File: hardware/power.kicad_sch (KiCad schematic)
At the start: 0 parts

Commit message: schematic: power and imu sheets drawn (ERC 0 on each sheet; P4-1/2/3/7/9/12/17/19 closed in block notes)
Co-Authored-By: Claude Opus 5.5 <noreply@anthropic.com>
Claude-Session: https://claude.ai/code/session_01RFaS5jnC9tnPam9GBgmGnG
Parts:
- added C1, C10, C11, C2, C7, C8, C9: 22uF, lib:C_0603_1608Metric_W, symbol Device:C
- added C12, C128, C13, C15, C30: 10uF, lib:C_0402_1005Metric_W, symbol Device:C
- added C129, C131, C6: 100nF, lib:C_0201_0603Metric_W, symbol Device:C
- added C14, C17, C5: 1uF, lib:C_0201_0603Metric_W, symbol Device:C
- added C16: 10nF, lib:C_0201_0603Metric_W, symbol Device:C
- added D1: SMF5.0A, lib:SOD-123FL_L2.7-W1.8-LS3.7-RD_Dense, symbol Device:D_Zener
- added D2: BAS16LD, lib:Nexperia_SOD882D, symbol Device:D
- added FB1: 120R@100MHz 0.9A, lib:L_0201_0603Metric_W, symbol Device:FerriteBead
- added L1: 0.68uH 6.5A, lib:IND-SMD_L2.5-W2.0_FTC252012, symbol Device:L
- added R1: 0.5mR 2W, lib:R_1206_Kelvin_4Pad_NetTie_HCS1206_Dense, symbol Device:R_Shunt
- added R10: 18k, lib:R_0201_0603Metric_W, symbol Device:R
- added R11: 2.4k, lib:R_0201_0603Metric_W, symbol Device:R
- added R2, R3: 1k, lib:R_0201_0603Metric_W, symbol Device:R
- added R4: 47k, lib:R_0201_0603Metric_W, symbol Device:R
- added R5: 6.2k, lib:R_0201_0603Metric_W, symbol Device:R
- added R7: 27.4k, lib:R_0201_0603Metric_W, symbol Device:R
- added R8: 10k, lib:R_0201_0603Metric_W, symbol Device:R
- added R87: 510k, lib:R_0201_0603Metric_W, symbol Device:R
- added R9: 33k, lib:R_0201_0603Metric_W, symbol Device:R
- added U1: INA186A3, lib:SOT-363_SC-70-6_Dense, symbol OpenDrone:INA186A3IDCKR
- added U2: TPS61022, lib:TI_VQFN-HR-7_2x2mm_RWU, symbol lib:TPS61022RWUR
- added U24: SGM40661, lib:WLCSP-6_L1.30-W0.94-P0.40_SGM40661, symbol lib:SGM40661YG
- added U3: TPS2116, lib:TI_SOT-583_DRL, symbol lib:TPS2116DRLR
- added U4: LP5912-3.3, lib:WSON-6-1EP_2x2mm_P0.65mm_EP1x1.6mm_Dense, symbol OpenDrone:LP5912-3.3DRVR
- added U5: TPS22810, lib:SOT-23-6_L2.9-W1.6-P0.95-LS2.8-BR_Dense, symbol lib:TPS22810DBVR
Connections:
- new net: C16.1, U5.4 (CT)
- new net +3V3: C14.1, C6.1, U1.3 (VS), U4.1 (OUT)
- new net +5V: C12.1, C13.1, FB1.1, U3.2 (VOUT), U3.7 (VOUT), U4.4 (EN), U4.6 (IN)
- new net +5V_BST: C10.1, C11.1, C17.1, C8.1, C9.1, R4.1, U2.3 (VOUT), U2.6 (MODE), U3.6 (VIN2), U5.1 (VIN)
- new net +5V_CAM: C15.1, FB1.2
- new net +5V_HD: R87.1, U5.5 (QOD), U5.6 (VOUT)
- new net +5V_USB: C128.1, R7.1, U24.A1 (OUT), U24.B1 (OUT), U3.3 (VIN1), U3.5 (MODE)
- new net +BATT: C30.1, C7.1, L1.1, R1.4, R9.1, U2.5 (EN), U2.7 (VIN)
- new net +BATT_IN: C1.1, C2.1, D1.1 (K), R1.1
- new net CURR_SENSE: U1.6 (OUT)
- new net GND: C1.2, C10.2, C11.2, C12.2, C128.2, C129.2, C13.2, C131.2, C14.2, C15.2, C16.2, C17.2, C2.2, C30.2, C6.2, C7.2, C8.2, C9.2, D1.2 (A), R10.2, R11.2, R5.2, R8.2, U1.1 (REF), U1.2 (GND), U2.1 (GND), U24.C1 (GND), U24.C2 (OVLO), U3.1 (GND), U4.5 (GND), U4.7 (EP), U5.2 (GND)
- new net HD_EN: D2.1 (K), R11.1
- new net SHUNT_SENSE_N: R1.3, R3.1
- new net SHUNT_SENSE_N_RC: C5.1, R3.2, U1.5 (-IN)
- new net SHUNT_SENSE_P: R1.2, R2.1
- new net SHUNT_SENSE_P_RC: C5.2, R2.2, U1.4 (+IN)
- new net U2_FB: R4.2, R5.1, U2.4 (FB)
- new net U2_SW: L1.2, U2.2 (SW)
- new net U3_PR1: R7.2, R8.1, U3.4 (PR1)
- new net U5_EN: C129.1, D2.2 (A), R10.1, R87.2, R9.2, U5.3 (EN/UVLO)
- new net VBUS: C131.1, U24.A2 (IN), U24.B2 (IN)
- no-connect marks 0 -> 3
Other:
- note added: "3.3 V LDO FOR FC + RX"
- note added: "5 V BOOST TPS61022"
- note added: "5 V POWER MUX TPS2116"
- note added: "BATTERY CURRENT SENSE"
- note added: "BATTERY INPUT AND TVS"
- note added: "CAMERA 5 V FILTER"
- note added: "ESC3 EFM8 VDD BULK"
- note added: "O4 LITE HD SUPPLY SWITCH TPS22810"
- note added: "SHEET NOTES"
- note added: "USB INLET OVP SGM40661"

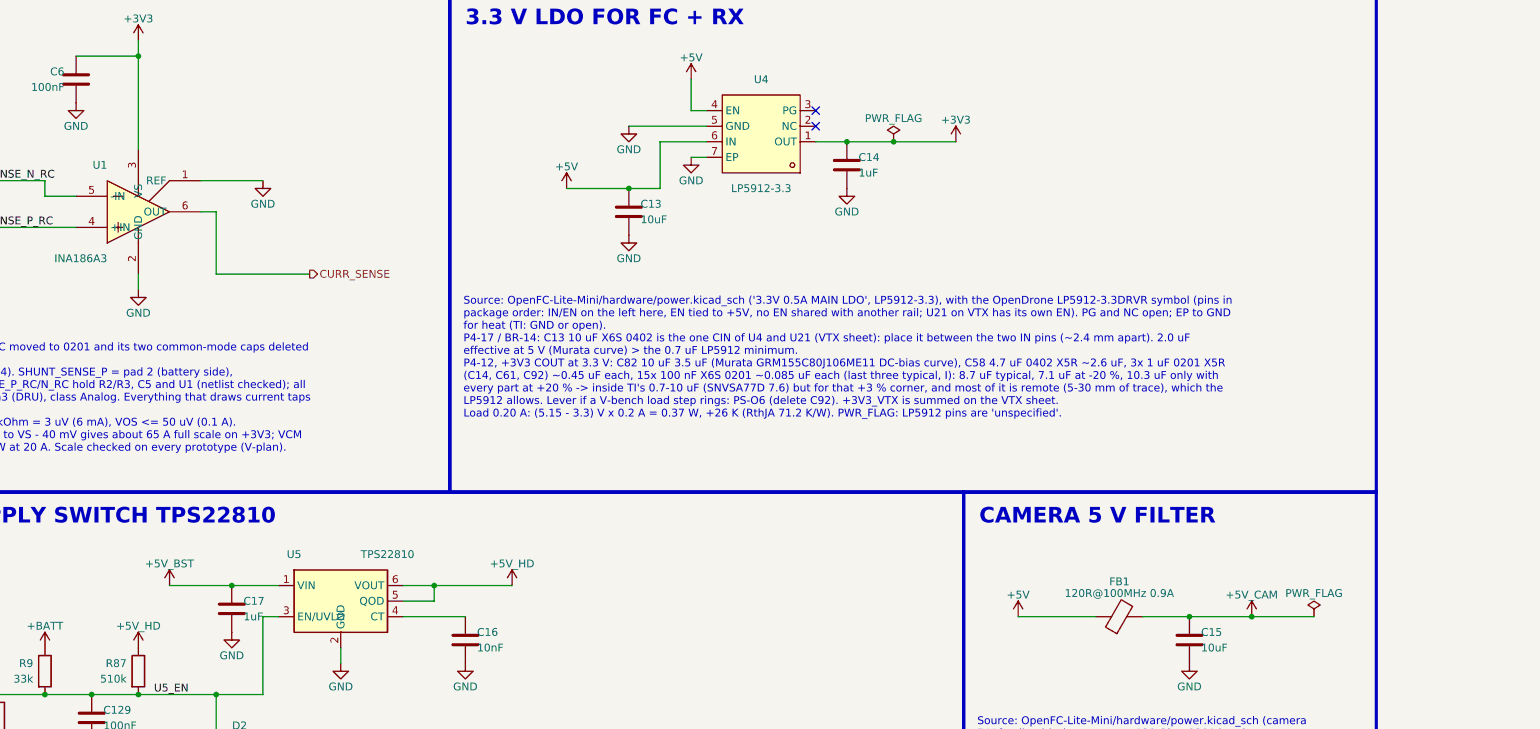
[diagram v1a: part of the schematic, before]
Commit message: wip: schematic integration in progress (saved after container restart)
Co-Authored-By: Claude Opus 5.5 <noreply@anthropic.com>
Claude-Session: https://claude.ai/code/session_01RFaS5jnC9tnPam9GBgmGnG
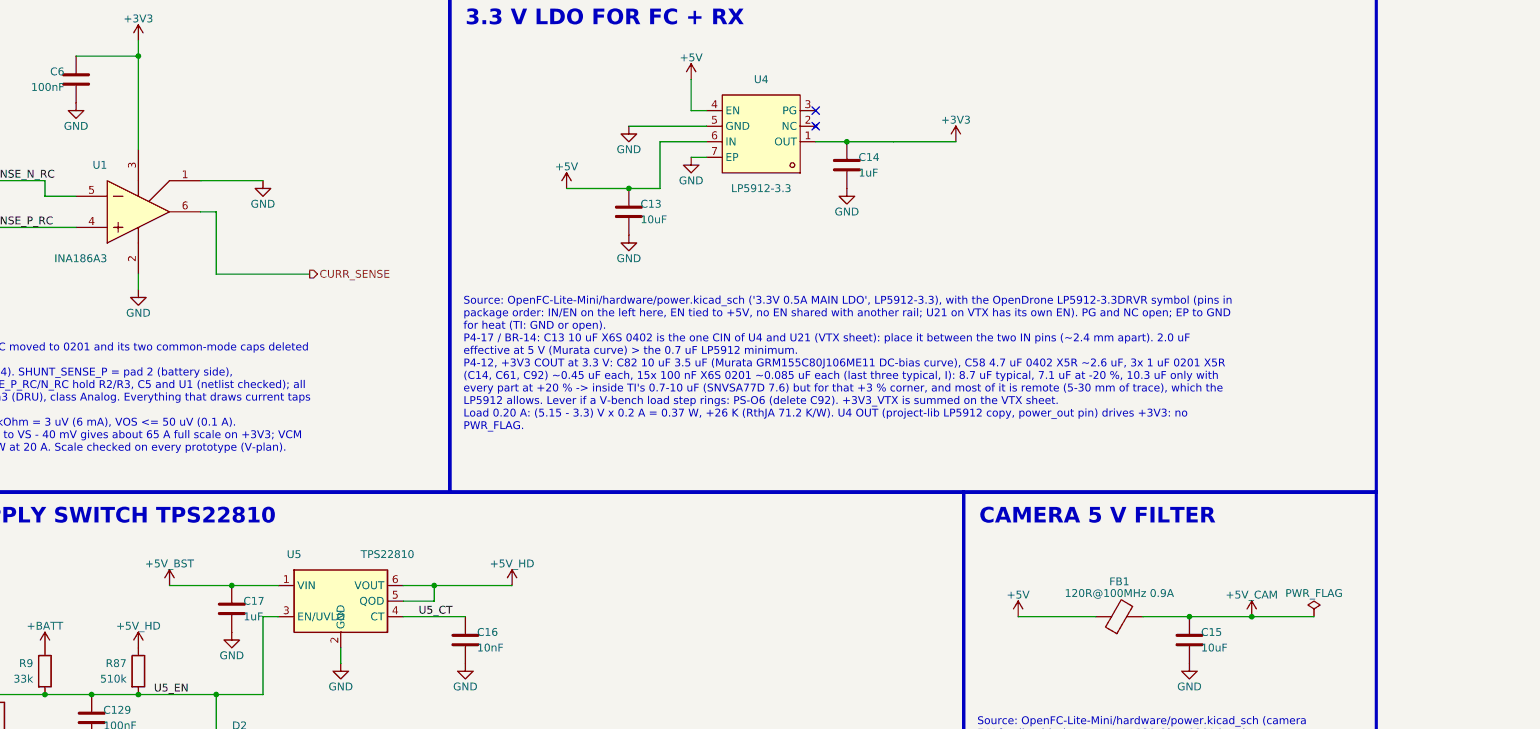
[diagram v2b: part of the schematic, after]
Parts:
- C12, C15: LCSC (none) -> C237279
- U1: symbol OpenDrone:INA186A3IDCKR -> lib:INA186A3IDCKR
- U4: symbol OpenDrone:LP5912-3.3DRVR -> lib:LP5912-3.3DRVR
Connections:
- net U5_CT: now reaches C16.1, U5.4 (CT)

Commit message: schematic: integrated (ERC 0 errors / 2 justified warnings; check_netlist 7/7; conventions 0 FAIL; visual 0 hits; 268/268 refs match bom_plan; FC+RX pin maps match PINMAP)
Co-Authored-By: Claude Opus 5.5 <noreply@anthropic.com>
Claude-Session: https://claude.ai/code/session_01RFaS5jnC9tnPam9GBgmGnG
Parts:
- removed C17: 1uF, lib:C_0201_0603Metric_W, symbol Device:C
- removed C30: 10uF, lib:C_0402_1005Metric_W, symbol Device:C
- L1: Manufacturer cjiang -> Changjiang Microelectronics (CJiang)
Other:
- note removed: "ESC3 EFM8 VDD BULK"
